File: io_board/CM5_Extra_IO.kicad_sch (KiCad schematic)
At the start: 0 parts

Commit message: Added all necessary IO connectors.
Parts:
- added J10, J12, J13, J15, J9: BM04B-GHS-TBT_LF__SN_, BM04B-GHS-TBT_LF__SN_:BM04BGHSTBTLFSN, symbol BM04B-GHS-TBT_LF__SN_:BM04B-GHS-TBT_LF__SN_
- added J17: BM06B-GHS-TBT_LF__SN_, BM06B-GHS-TBT_LF__SN_:BM06BGHSTBTLFSN, symbol BM06B-GHS-TBT_LF__SN_:BM06B-GHS-TBT_LF__SN_
- added J6: USB1135-15-9-L-B, USB1135-15-9-L-B:USB1135159LB, symbol USB1135-15-9-L-B:USB1135-15-9-L-B
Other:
- note added: "I2C"
- note added: "PWM"
- note added: "SPI"
- note added: "Serial"
- note added: "USB 3.0"
- company: (none) -> Ilias Kringos - March 2026
- title: (none) -> Compute Module 5 IO Board - Extra IO

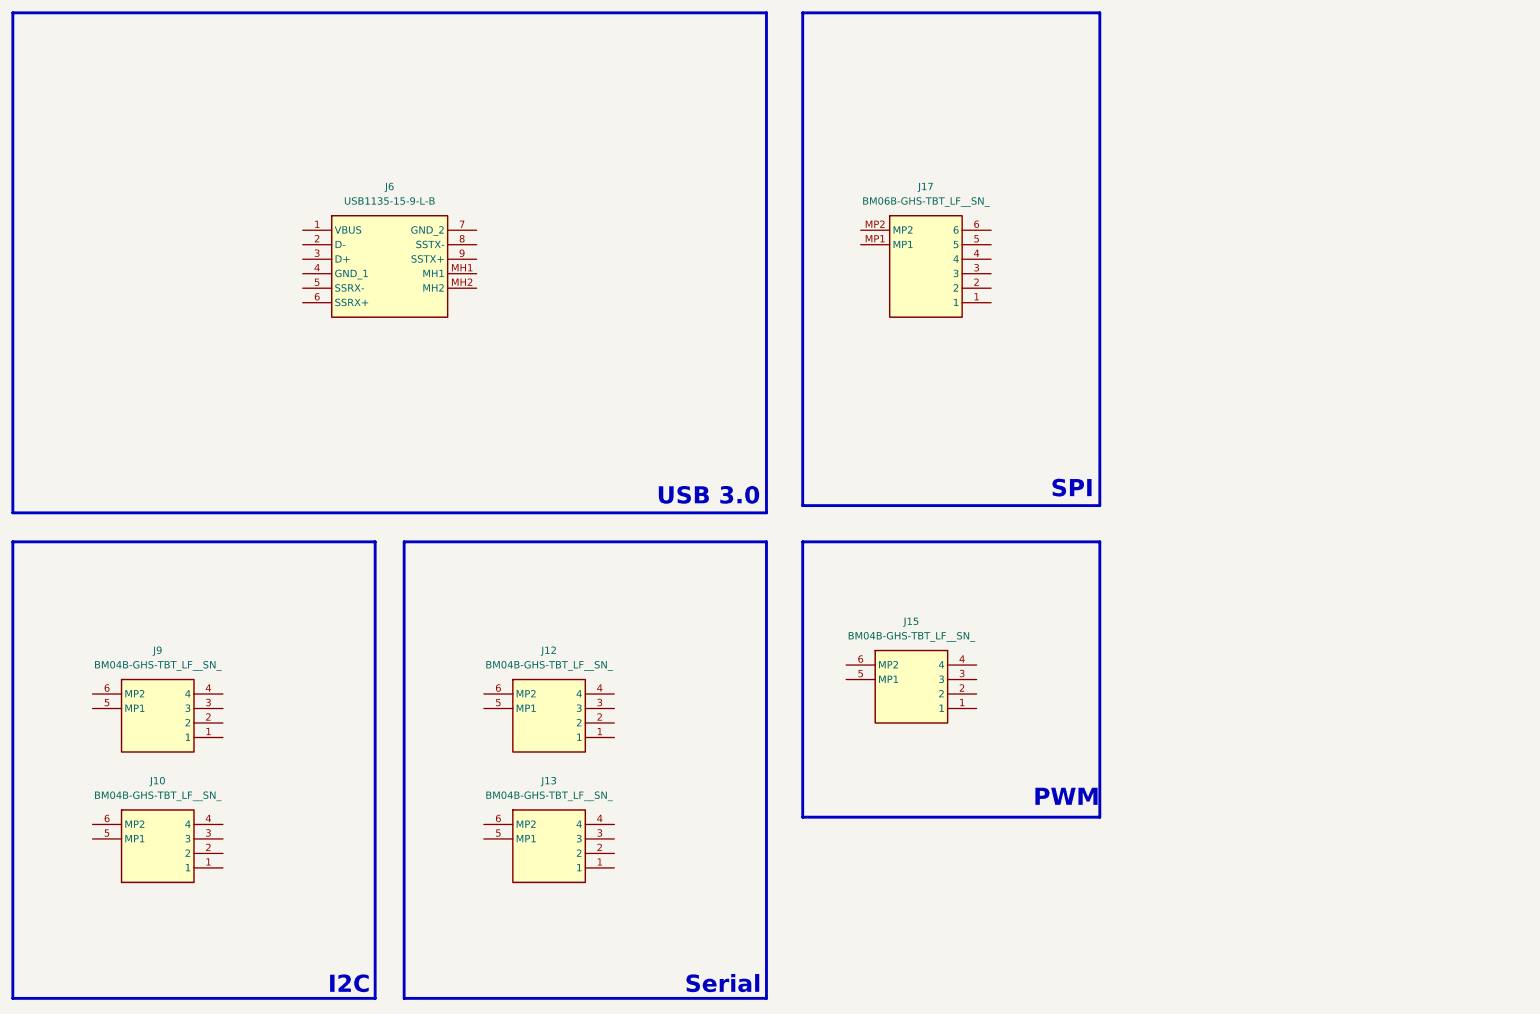
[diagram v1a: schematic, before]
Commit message: Assigned pins to I2C, UART, PWM, SPI ports.
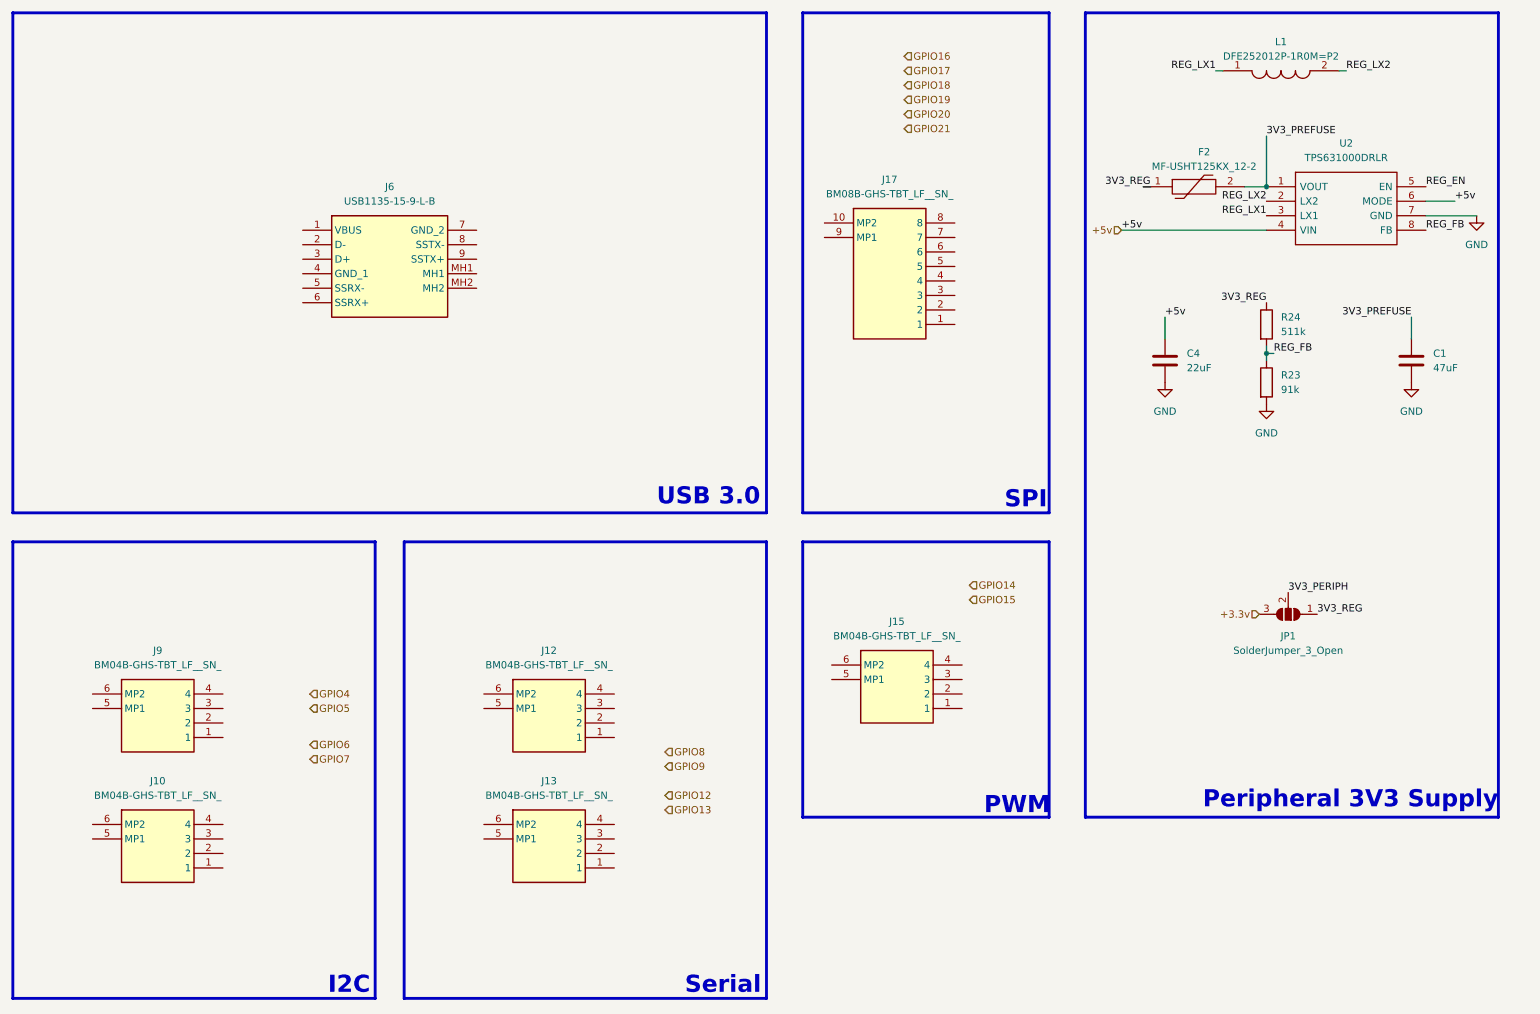
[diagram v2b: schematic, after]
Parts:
- removed J17: BM06B-GHS-TBT_LF__SN_, BM06B-GHS-TBT_LF__SN_:BM06BGHSTBTLFSN, symbol BM06B-GHS-TBT_LF__SN_:BM06B-GHS-TBT_LF__SN_
- added C1: 47uF, Capacitor_SMD:C_0805_2012Metric_Pad1.18x1.45mm_HandSolder, symbol Device:C
- added C4: 22uF, Capacitor_SMD:C_0603_1608Metric_Pad1.08x0.95mm_HandSolder, symbol Device:C
- added F2: MF-USHT125KX_12-2, MF-USHT125KX_12-2:MFUSHT125KX122, symbol MF-USHT125KX_12-2:MF-USHT125KX_12-2
- added J17: BM08B-GHS-TBT_LF__SN_, BM08B-GHS-TBT_LF__SN_:BM08BGHSTBTLFSN, symbol BM08B-GHS-TBT_LF__SN_:BM08B-GHS-TBT_LF__SN_
- added JP1: SolderJumper_3_Open, Jumper:SolderJumper-3_P2.0mm_Open_TrianglePad1.0x1.5mm, symbol Jumper:SolderJumper_3_Open
- added L1: DFE252012P-1R0M=P2, DFE2HCAH1R0MJ0L, symbol DFE252012P-1R0M=P2:DFE252012P-1R0M=P2
- added R23: 91k, Resistor_SMD:R_0805_2012Metric_Pad1.20x1.40mm_HandSolder, symbol Device:R
- added R24: 511k, Resistor_SMD:R_0805_2012Metric_Pad1.20x1.40mm_HandSolder, symbol Device:R
- added U2: TPS631000DRLR, SOTFL50P160X60-8N, symbol TPS631000DRLR:TPS631000DRLR
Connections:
- new net +3.3v: JP1.3 (B)
- new net +5v: C4.1, U2.4 (VIN), U2.6 (MODE)
- new net 3V3_PERIPH: JP1.2 (C)
- new net 3V3_PREFUSE: C1.1, F2.2, U2.1 (VOUT)
- new net 3V3_REG: F2.1, JP1.1 (A), R24.1
- new net GND: C1.2, C4.2, R23.2, U2.7 (GND)
- new net REG_EN: U2.5 (EN)
- new net REG_FB: R23.1, R24.2, U2.8 (FB)
- new net REG_LX1: L1.1, U2.3 (LX1)
- new net REG_LX2: L1.2, U2.2 (LX2)
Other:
- note added: "Peripheral 3V3 Supply"
- moved on the sheet: J15

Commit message: Connected I2C, Serial, PWM, SPI. USB3, Ethernet, PCIE left to do.
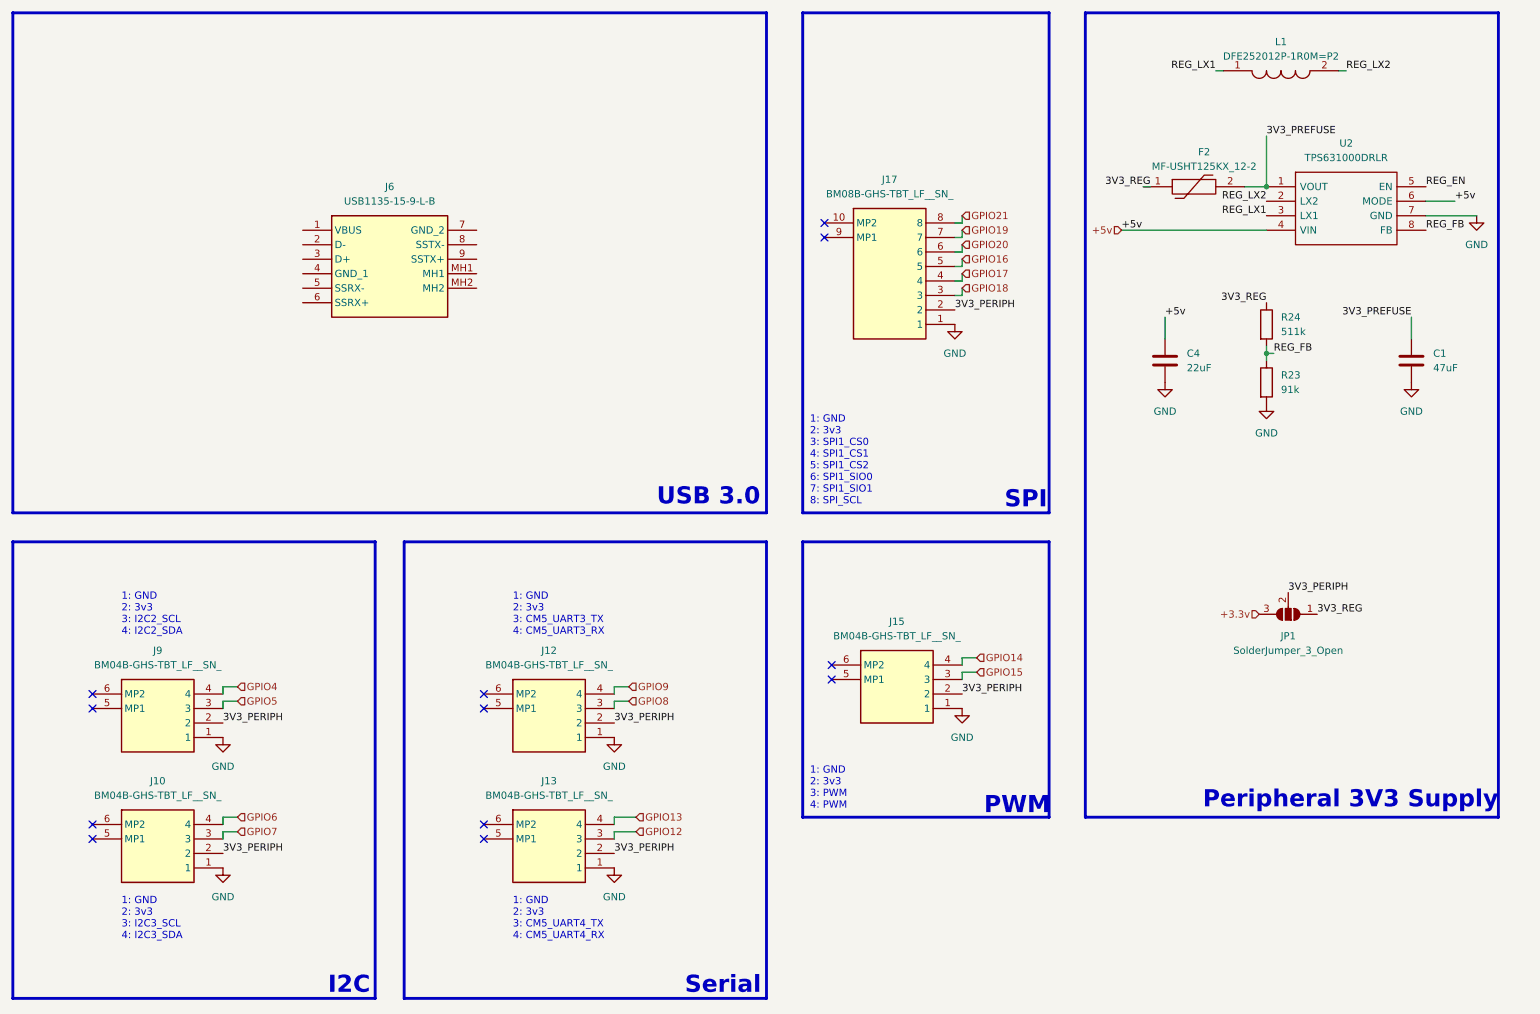
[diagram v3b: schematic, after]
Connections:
- net 3V3_PERIPH: now also J10.2, J12.2, J13.2, J15.2, J17.2, J9.2
- net GND: now also J10.1, J12.1, J13.1, J15.1, J17.1, J9.1
- net GPIO12: now also J13.3
- net GPIO13: now also J13.4
- net GPIO14: now also J15.4
- net GPIO15: now also J15.3
- net GPIO16: now also J17.5
- net GPIO17: now also J17.4
- net GPIO18: now also J17.3
- net GPIO19: now also J17.7
- net GPIO20: now also J17.6
- net GPIO21: now also J17.8
- net GPIO4: now also J9.4
- net GPIO5: now also J9.3
- net GPIO6: now also J10.4
- net GPIO7: now also J10.3
- net GPIO8: now also J12.3
- net GPIO9: now also J12.4
- no-connect marks 0 -> 12
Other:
- note added: "1: GND 2: 3v3 3: CM5_UART3_TX 4: CM5_UART3_RX"
- note added: "1: GND 2: 3v3 3: CM5_UART4_TX 4: CM5_UART4_RX"
- note added: "1: GND 2: 3v3 3: I2C2_SCL 4: I2C2_SDA"
- note added: "1: GND 2: 3v3 3: I2C3_SCL 4: I2C3_SDA"
- note added: "1: GND 2: 3v3 3: PWM 4: PWM"
- note added: "1: GND 2: 3v3 3: SPI1_CS0 4: SPI1_CS1 5: SPI1_CS2 6: SPI1_SIO0 7: SPI1_SIO1 8: SPI_SCL"

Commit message: Connected USB 3.0 and added part number for PCIe.
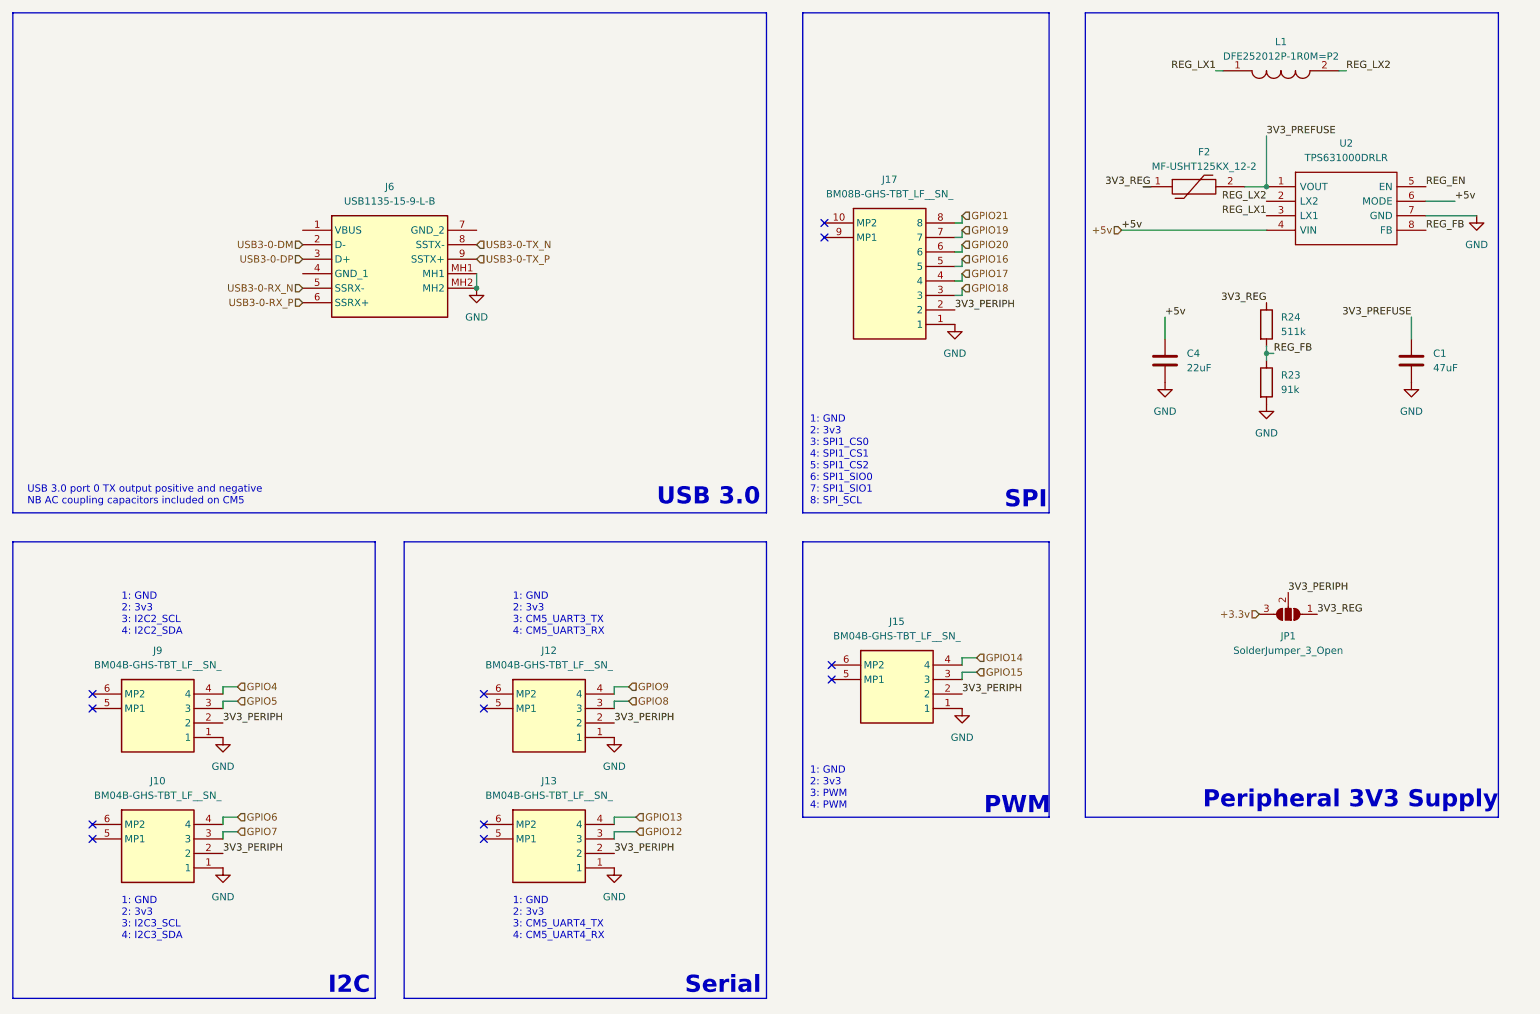
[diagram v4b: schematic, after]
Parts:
- L1: footprint DFE2HCAH1R0MJ0L -> DFE252012P-1R0M=P2:DFE2HCAH1R0MJ0L
- U2: footprint SOTFL50P160X60-8N -> TPS631000DRLR:SOTFL50P160X60-8N
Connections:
- net GND: now also J6.MH1, J6.MH2
- net USB3-0-DM: now reaches J6.2 (D-)
- net USB3-0-DP: now reaches J6.3 (D+)
- net USB3-0-RX_N: now reaches J6.5 (SSRX-)
- net USB3-0-RX_P: now reaches J6.6 (SSRX+)
- net USB3-0-TX_N: now reaches J6.8 (SSTX-)
- net USB3-0-TX_P: now reaches J6.9 (SSTX+)
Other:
- note added: "USB 3.0 port 0 TX output positive and negative NB AC coupling capacitors included on CM5"
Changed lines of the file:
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@@
 		(end 200.66 160.02)
 		(stroke
-			(width 0.5)
+			(width 0)
 			(type solid)
 		)
@@
 		(end 200.66 106.68)
 		(stroke
-			(width 0.5)
+			(width 0)
 			(type solid)
 		)
@@
 		(end 151.13 106.68)
 		(stroke
-			(width 0.5)
+			(width 0)
 			(type solid)
 		)
@@
 		(end 279.4 160.02)
 		(stroke
-			(width 0.5)
+			(width 0)
 			(type solid)
 		)
@@
 		(end 151.13 191.77)
 		(stroke
-			(width 0.5)
+			(width 0)
 			(type solid)
 		)
@@
 		(end 82.55 191.77)
 		(stroke
-			(width 0.5)
+			(width 0)
 			(type solid)
 		)
@@
 				(bold yes)
 			)
+		)
+	)
+	(text "USB 3.0 port 0 TX output positive and negative\nNB AC coupling capacitors included on CM5"
+		(exclude_from_sim no)
+		(at 21.59 105.41 0)
+		(effects
+			(font
+				(size 1.27 1.27)
+			)
+			(justify left bottom)
 		)
 	)
@@
 	)
 	(junction
+		(at 100.33 67.31)
+		(diameter 0)
+		(color 0 0 0 0)
+	)
+	(junction
 		(at 238.76 49.53)
 		(diameter 0)
@@
 	(wire
 		(pts
+			(xy 100.33 64.77) (xy 100.33 67.31)
+		)
+		(stroke
+			(width 0)
+			(type default)
+		)
+	)
+	(wire
+		(pts
 			(xy 124.46 139.7) (xy 124.46 140.97)
 		)
@@
 		)
 	)
+	(hierarchical_label "USB3-0-TX_P"
+		(shape input)
+		(at 100.33 62.23 0)
+		(effects
+			(font
+				(size 1.27 1.27)
+			)
+			(justify left)
+		)
+	)
 	(hierarchical_label "GPIO13"
 		(shape input)
@@
 		)
 	)
+	(hierarchical_label "USB3-0-DP"
+		(shape input)
+		(at 69.85 62.23 180)
+		(effects
+			(font
+				(size 1.27 1.27)
+			)
+			(justify right)
+		)
+	)
 	(hierarchical_label "GPIO20"
 		(shape input)
@@
 		)
 	)
+	(hierarchical_label "USB3-0-DM"
+		(shape input)
+		(at 69.85 59.69 180)
+		(effects
+			(font
+				(size 1.27 1.27)
+			)
+			(justify right)
+		)
+	)
 	(hierarchical_label "GPIO17"
 		(shape input)
@@
 		)
 	)
+	(hierarchical_label "USB3-0-RX_N"
+		(shape input)
+		(at 69.85 67.31 180)
+		(effects
+			(font
+				(size 1.27 1.27)
+			)
+			(justify right)
+		)
+	)
+	(hierarchical_label "USB3-0-RX_P"
+		(shape input)
+		(at 69.85 69.85 180)
+		(effects
+			(font
+				(size 1.27 1.27)
+			)
+			(justify right)
+		)
+	)
 	(hierarchical_label "GPIO8"
 		(shape input)
 		(at 127 139.7 0)
+		(effects
+			(font
+				(size 1.27 1.27)
+			)
+			(justify left)
+		)
+	)
+	(hierarchical_label "USB3-0-TX_N"
+		(shape input)
+		(at 100.33 59.69 0)
 		(effects
 			(font
@@
 	)
 	(symbol
+		(lib_id "power:GND")
+		(at 100.33 67.31 0)
+		(unit 1)
+		(exclude_from_sim no)
+		(in_bom yes)
+		(on_board yes)
+		(dnp no)
+		(fields_autoplaced yes)
+		(property "Reference" "#PWR018"
+			(at 100.33 73.66 0)
+			(effects
+				(font
+					(size 1.27 1.27)
+				)
+				(hide yes)
+			)
+		)
+		(property "Value" "GND"
+			(at 100.33 72.39 0)
+			(effects
+				(font
+					(size 1.27 1.27)
+				)
+			)
+		)
+		(property "Footprint" ""
+			(at 100.33 67.31 0)
+			(effects
+				(font
+					(size 1.27 1.27)
+				)
+				(hide yes)
+			)
+		)
+		(property "Datasheet" ""
+			(at 100.33 67.31 0)
+			(effects
+				(font
+					(size 1.27 1.27)
+				)
+				(hide yes)
+			)
+		)
+		(property "Description" "Power symbol creates a global label with name \"GND\" , ground"
+			(at 100.33 67.31 0)
+			(effects
+				(font
+					(size 1.27 1.27)
+				)
+				(hide yes)
+			)
+		)
+		(pin "1"
+		)
+		(instances
+			(project "CM5IO"
+				(path "/e63e39d7-6ac0-4ffd-8aa3-1841a4541b55/1a000998-d290-4943-9ac8-07307b2fbf9f"
+					(reference "#PWR018")
+					(unit 1)
+				)
+			)
+		)
+	)
+	(symbol
 		(lib_id "TPS631000DRLR:TPS631000DRLR")
 		(at 238.76 49.53 0)
@@
 			)
 		)
-		(property "Footprint" "SOTFL50P160X60-8N"
+		(property "Footprint" "TPS631000DRLR:SOTFL50P160X60-8N"
 			(at 262.89 46.99 0)
 			(effects
@@
 			)
 		)
-		(property "Footprint" "DFE2HCAH1R0MJ0L"
+		(property "Footprint" "DFE252012P-1R0M=P2:DFE2HCAH1R0MJ0L"
 			(at 247.65 27.94 0)
 			(effects
